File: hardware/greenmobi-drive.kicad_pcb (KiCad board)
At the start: 4 copper layers, 26 parts, among them J1 USB_C_Receptacle_USB2.0_14P, J2 Debug, J3 BAT, Q1 NMOS, SW1 RESET, SW2 BOOT, U1 STM32F405RGTx, Y1 8MHz

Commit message: Add a board edge to test CI
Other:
- board outline added: 87.1 x 77.9 mm
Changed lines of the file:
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@@
 			(psa4output no)
 			(plot_black_and_white yes)
-			(plotinvisibletext no)
 			(sketchpadsonfab no)
 			(plotpadnumbers no)
@@
 		(layer "Dwgs.User")
 	)
+	(gr_rect
+		(start 100.9 42.3)
+		(end 188 120.2)
+		(stroke
+			(width 0.05)
+			(type default)
+		)
+		(fill no)
+		(layer "Edge.Cuts")
+	)
 	(via

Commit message: half bridges
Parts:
- added C2: 2.2u, Capacitor_SMD:C_0402_1005Metric, F.Cu at (139.7, 54.8)
- added C29: 100n, Capacitor_SMD:C_1206_3216Metric, F.Cu at (123.7, 65.4)
- added C3: 2.2u, Capacitor_SMD:C_0402_1005Metric, F.Cu at (148.3, 54.8)
- added C33: 1u, Capacitor_SMD:C_0402_1005Metric, F.Cu at (133.6, 58.1)
- added C34: 4.7u, Capacitor_SMD:C_0805_2012Metric, F.Cu at (118.6, 58.6)
- added C35: 4.7u, Capacitor_SMD:C_0805_2012Metric, F.Cu at (118.6, 61.7)
- added C36: 1u, Capacitor_SMD:C_0402_1005Metric, F.Cu at (133.6, 60.1)
- added C37: 4.7u, Capacitor_SMD:C_0805_2012Metric, F.Cu at (118.6, 64.7)
- added D1: YELLOW, LED_SMD:LED_0805_2012Metric, F.Cu at (139.1, 76.7)
- added D2: RED, LED_SMD:LED_0805_2012Metric, F.Cu at (139.1, 79.8)
- added D3: GREEN, LED_SMD:LED_0805_2012Metric, F.Cu at (139.1, 82.8)
- added D4: SS34, Diode_SMD:D_SMA, F.Cu at (143.7, 96.7)
- added D5: SS34, Diode_SMD:D_SMA, F.Cu at (240.1, 85.1)
- added D6: SS34, Diode_SMD:D_SMA, F.Cu at (210.6, 85.1)
- added J2: GND, MountingHole:MountingHole_5.3mm_M5_DIN965_Pad, F.Cu at (127.2, 73.5)
- added J5: CAN, Connector_JST:JST_GH_SM04B-GHS-TB_1x04-1MP_P1.25mm_Horizontal, F.Cu at (144.1, 48.2)
- added J7: Phase_OUT, MountingHole:MountingHole_5.3mm_M5_DIN965_Pad, F.Cu at (136.4, 109.0)
- added J8: Phase_OUT, MountingHole:MountingHole_5.3mm_M5_DIN965_Pad, F.Cu at (241.4, 77.5)
- added J9: Phase_OUT, MountingHole:MountingHole_5.3mm_M5_DIN965_Pad, F.Cu at (211.9, 77.5)
- added L2: L, Inductor_SMD:L_KOHERelec_MDA7030, F.Cu at (131.0, 52.9)
- added Q10: AGM015N10LL, Package_TO_SOT_SMD:Infineon_PG-HSOF-8-1_ThermalVias, F.Cu at (228.6, 93.0)
- added Q11: AGM015N10LL, Package_TO_SOT_SMD:Infineon_PG-HSOF-8-1_ThermalVias, F.Cu at (228.6, 104.6)
- added Q12: AGM015N10LL, Package_TO_SOT_SMD:Infineon_PG-HSOF-8-1_ThermalVias, F.Cu at (228.6, 116.3)
- added Q13: AGM015N10LL, Package_TO_SOT_SMD:Infineon_PG-HSOF-8-1_ThermalVias, F.Cu at (199.1, 57.9)
- added Q14: AGM015N10LL, Package_TO_SOT_SMD:Infineon_PG-HSOF-8-1_ThermalVias, F.Cu at (199.1, 69.6)
- added Q15: AGM015N10LL, Package_TO_SOT_SMD:Infineon_PG-HSOF-8-1_ThermalVias, F.Cu at (199.1, 81.3)
- added Q16: AGM015N10LL, Package_TO_SOT_SMD:Infineon_PG-HSOF-8-1_ThermalVias, F.Cu at (199.1, 93.0)
- added Q17: AGM015N10LL, Package_TO_SOT_SMD:Infineon_PG-HSOF-8-1_ThermalVias, F.Cu at (199.1, 104.6)
- added Q18: AGM015N10LL, Package_TO_SOT_SMD:Infineon_PG-HSOF-8-1_ThermalVias, F.Cu at (199.1, 116.3)
- added Q2: AGM015N10LL, Package_TO_SOT_SMD:Infineon_PG-HSOF-8-1_ThermalVias, F.Cu at (158.2, 111.1)
- added Q3: AGM015N10LL, Package_TO_SOT_SMD:Infineon_PG-HSOF-8-1_ThermalVias, F.Cu at (168.9, 97.2)
- added Q4: AGM015N10LL, Package_TO_SOT_SMD:Infineon_PG-HSOF-8-1_ThermalVias, F.Cu at (168.9, 111.1)
- added Q5: AGM015N10LL, Package_TO_SOT_SMD:Infineon_PG-HSOF-8-1_ThermalVias, F.Cu at (179.7, 97.2)
- added Q6: AGM015N10LL, Package_TO_SOT_SMD:Infineon_PG-HSOF-8-1_ThermalVias, F.Cu at (179.7, 111.1)
- added Q7: AGM015N10LL, Package_TO_SOT_SMD:Infineon_PG-HSOF-8-1_ThermalVias, F.Cu at (228.6, 57.9)
- added Q8: AGM015N10LL, Package_TO_SOT_SMD:Infineon_PG-HSOF-8-1_ThermalVias, F.Cu at (228.6, 69.6)
- added Q9: AGM015N10LL, Package_TO_SOT_SMD:Infineon_PG-HSOF-8-1_ThermalVias, F.Cu at (228.6, 81.3)
- added R20: 56k, Resistor_SMD:R_0402_1005Metric, F.Cu at (160.0, 79.5)
- added R23: 5.1k, Resistor_SMD:R_0402_1005Metric, F.Cu at (160.0, 81.4)
- added R24: 0.2m, Resistor_SMD:R_4020_10251Metric, F.Cu at (147.1, 108.9)
- added R25: 5.1k, Resistor_SMD:R_0402_1005Metric, F.Cu at (160.0, 83.4)
- added R29: 56k, Resistor_SMD:R_0402_1005Metric, F.Cu at (237.4, 88.4)
- added R3: 56k, Resistor_SMD:R_0402_1005Metric, F.Cu at (142.7, 76.2)
- added R32: 5.1k, Resistor_SMD:R_0402_1005Metric, F.Cu at (237.4, 90.4)
- added R33: 0.2m, Resistor_SMD:R_4020_10251Metric, F.Cu at (242.3, 68.7)
- added R34: 5.1k, Resistor_SMD:R_0402_1005Metric, F.Cu at (237.4, 92.4)
- added R38: 56k, Resistor_SMD:R_0402_1005Metric, F.Cu at (207.9, 88.4)
- added R41: 5.1k, Resistor_SMD:R_0402_1005Metric, F.Cu at (207.9, 90.4)
- added R42: 0.2m, Resistor_SMD:R_4020_10251Metric, F.Cu at (212.8, 68.7)
- added R43: 5.1k, Resistor_SMD:R_0402_1005Metric, F.Cu at (207.9, 92.4)
- added R44: 82.5k, Resistor_SMD:R_0402_1005Metric, F.Cu at (130.7, 58.1)
- added R45: R, Resistor_SMD:R_0402_1005Metric, F.Cu at (130.7, 60.1)
- added R46: R, Resistor_SMD:R_0402_1005Metric, F.Cu at (130.7, 62.1)
- added R47: R, Resistor_SMD:R_0402_1005Metric, F.Cu at (130.7, 64.1)
- added U1: TJA1051T-3, Package_SO:SOIC-8_3.9x4.9mm_P1.27mm, F.Cu at (144.0, 54.8)
- added U10: AMS1117-3.3, Package_TO_SOT_SMD:SOT-223-3_TabPin2, F.Cu at (121.3, 53.0)
- added U3: IRS21867S, Package_SO:SOIC-8_3.9x4.9mm_P1.27mm, F.Cu at (154.3, 81.8)
- added U4: INA240A2D, Package_SO:SOIC-8_3.9x4.9mm_P1.27mm, F.Cu at (213.4, 102.7)
- added U5: IRS21867S, Package_SO:SOIC-8_3.9x4.9mm_P1.27mm, F.Cu at (240.2, 55.4)
- added U6: INA240A2D, Package_SO:SOIC-8_3.9x4.9mm_P1.27mm, F.Cu at (240.2, 62.0)
- added U7: IRS21867S, Package_SO:SOIC-8_3.9x4.9mm_P1.27mm, F.Cu at (210.7, 55.4)
- added U8: INA240A2D, Package_SO:SOIC-8_3.9x4.9mm_P1.27mm, F.Cu at (210.7, 62.0)
- added U9: LM5163DDA, Package_SO:HSOP-8-1EP_3.9x4.9mm_P1.27mm_EP2.41x3.1mm_ThermalVias, F.Cu at (125.0, 60.5)
- J3: value BAT -> UBAT; footprint Connector_AMASS:AMASS_XT90PW-M_1x02_P10.90mm_Horizontal -> MountingHole:MountingHole_5.3mm_M5_DIN965_Pad
- Q1: value NMOS -> AGM015N10LL
- moved Q1 50.5 mm to (158.2, 97.2), turned to 90 degrees
- moved J3 12.4 mm to (129.3, 88.1), turned to 0 degrees
- moved R12 5.68 mm to (161.7, 66.0)
- moved C12 5.68 mm to (149.8, 56.9)
- moved C4 5.68 mm to (166.2, 72.9)
- moved C6 5.68 mm to (143.3, 61.0)
- moved C7 5.68 mm to (143.3, 66.5)
- moved C9 5.68 mm to (145.6, 68.6)
- moved R13 5.68 mm to (161.7, 60.9)
- moved SW1 5.68 mm to (165.2, 55.4)
- moved SW2 5.68 mm to (165.2, 70.4)
- moved Y1 5.68 mm to (143.3, 63.8)
- moved C10 5.68 mm to (160.5, 60.9)
- moved C13 5.68 mm to (149.8, 58.0)
- moved C14 5.68 mm to (159.4, 59.9)
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- renumbered C8 to C10, C2 to C11, C7 to C12, C3 to C13, C4 to C14, C5 to C15, C6 to C16, C10 to C4, C13 to C5, C12 to C6, C11 to C7, C9 to C8, C1 to C9, J1 to J4, J2 to J6, R4 to R12, R3 to R13, R1 to R15, R2 to R16, SW2 to SW1, SW1 to SW2, U1 to U2
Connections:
- J3 pad 1: GND -> /Regulators/BAT
- Q1 pad 1: unconnected-(Q1-D-Pad1) -> Net-(Q1-G)
- Q1 pad 2: unconnected-(Q1-G-Pad2) -> Net-(Q1-S)
- Q1 pad 3: unconnected-(Q1-S-Pad3) -> /Regulators/BAT
- U2 pad 10: unconnected-(U1-PC2-Pad10) -> /half-bridge2/Current_sense
- U2 pad 11: unconnected-(U1-PC3-Pad11) -> /mcu/Vin
- U2 pad 14: unconnected-(U1-PA0-Pad14) -> /half-bridge/Phase_V_sense
- U2 pad 15: unconnected-(U1-PA1-Pad15) -> /half-bridge1/Phase_V_sense
- U2 pad 16: unconnected-(U1-PA2-Pad16) -> /half-bridge2/Phase_V_sense
- U2 pad 17: unconnected-(U1-PA3-Pad17) -> /half-bridge/TEMP
- U2 pad 24: unconnected-(U1-PC4-Pad24) -> /mcu/TEMP_MOTOR
- U2 pad 26: unconnected-(U1-PB0-Pad26) -> /half-bridge1/TEMP
- U2 pad 27: unconnected-(U1-PB1-Pad27) -> /half-bridge2/TEMP
- U2 pad 34: unconnected-(U1-PB13-Pad34) -> /half-bridge/LOW
- U2 pad 35: unconnected-(U1-PB14-Pad35) -> /half-bridge1/LOW
- U2 pad 36: unconnected-(U1-PB15-Pad36) -> /half-bridge2/LOW
- U2 pad 37: unconnected-(U1-PC6-Pad37) -> /mcu/HALL1
- U2 pad 38: unconnected-(U1-PC7-Pad38) -> /mcu/HALL2
- U2 pad 39: unconnected-(U1-PC8-Pad39) -> /mcu/HALL3
- U2 pad 41: unconnected-(U1-PA8-Pad41) -> /half-bridge/HIGH
- U2 pad 42: unconnected-(U1-PA9-Pad42) -> /half-bridge1/HIGH
- U2 pad 43: unconnected-(U1-PA10-Pad43) -> /half-bridge2/HIGH
- U2 pad 57: unconnected-(U1-PB5-Pad57) -> /mcu/LED_GREEN
- U2 pad 59: unconnected-(U1-PB7-Pad59) -> /mcu/LED_RED
- U2 pad 61: unconnected-(U1-PB8-Pad61) -> /mcu/CAN_RX
- U2 pad 62: unconnected-(U1-PB9-Pad62) -> /mcu/CAN_TX
- U2 pad 8: unconnected-(U1-PC0-Pad8) -> /half-bridge/Current_sense
- U2 pad 9: unconnected-(U1-PC1-Pad9) -> /half-bridge1/Current_sense
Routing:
- net /mcu/CAN_RX: track 0.00 -> 13.7 mm
- net /mcu/CAN_TX: track 0.00 -> 7.40 mm
- net /CAN_P: track 0.00 -> 7.09 mm
- net /CAN_N: track 0.00 -> 7.06 mm
- net +5V: track 0.00 -> 2.64 mm, vias 0 -> 1
- net +3.3V: track 18.9 -> 21.3 mm
- net GND: track 0.00 -> 1.66 mm, vias 31 -> 33

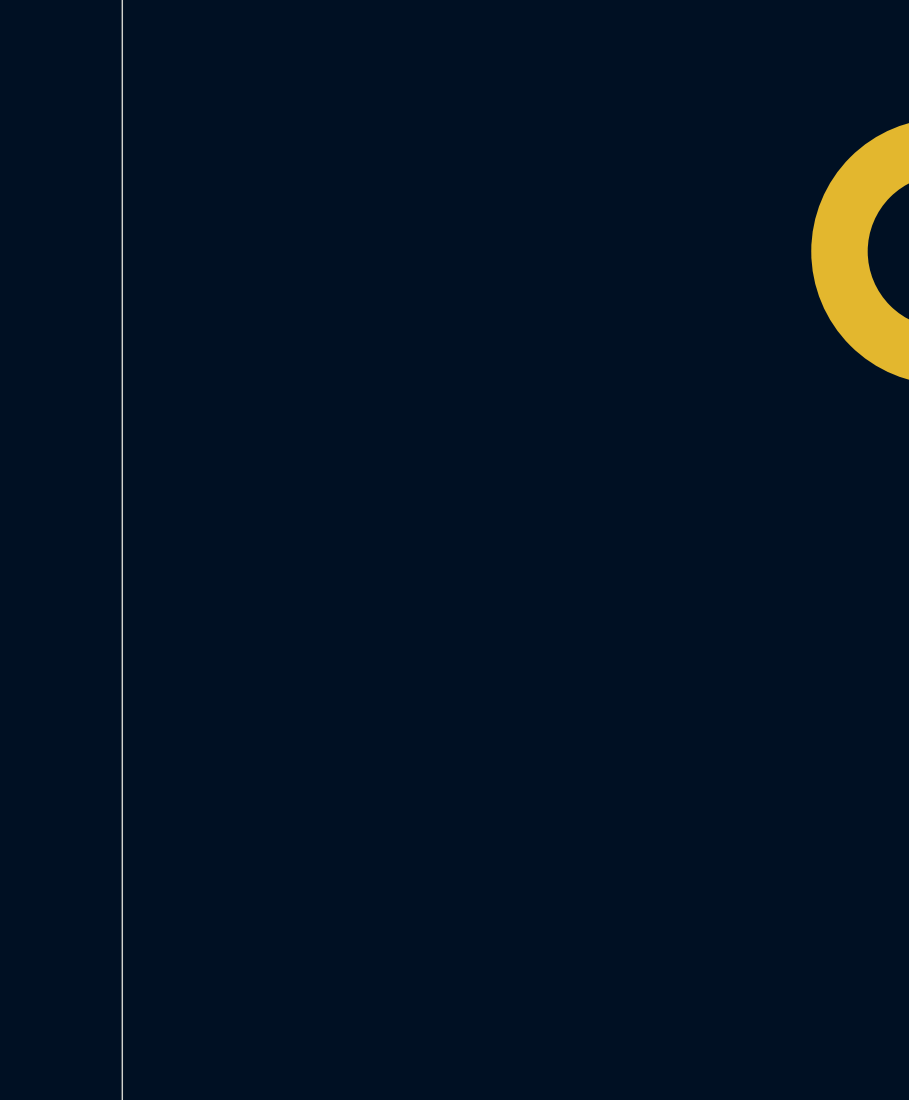
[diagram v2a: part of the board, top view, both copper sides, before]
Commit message: phase capacitors
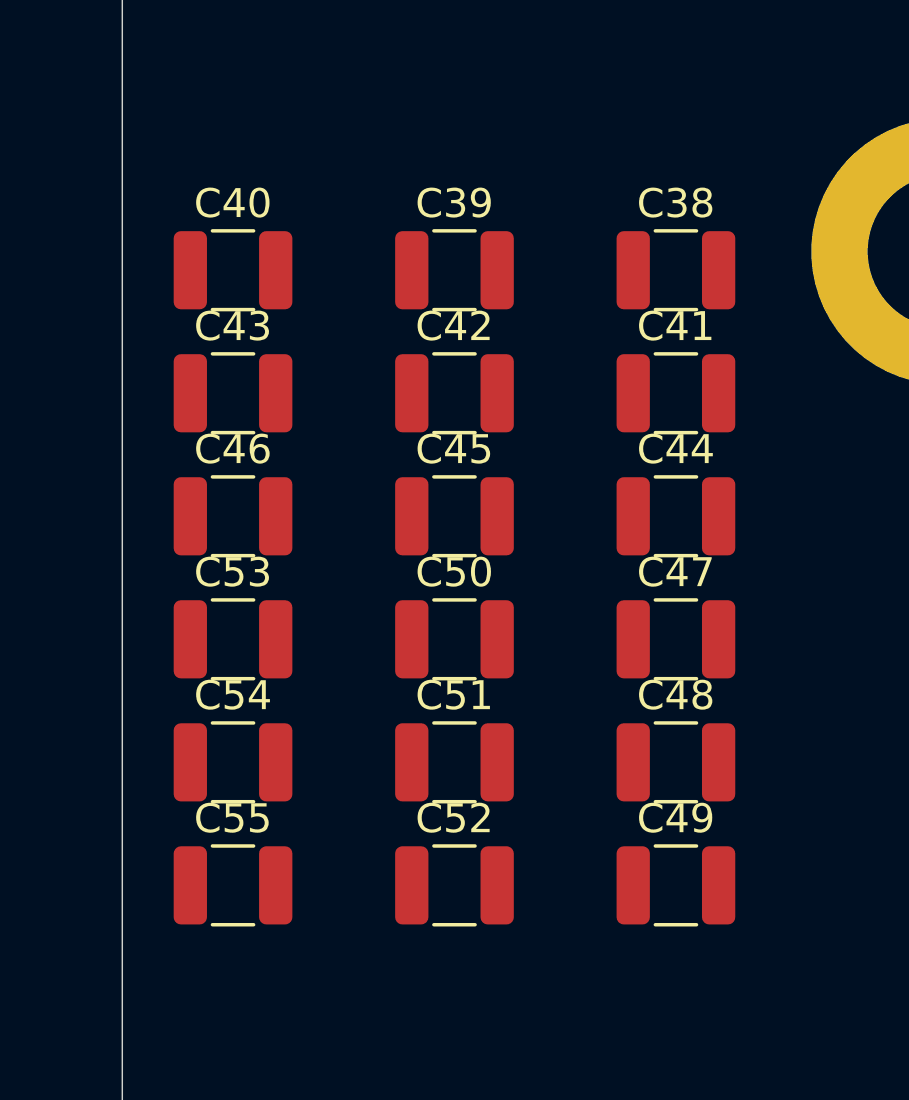
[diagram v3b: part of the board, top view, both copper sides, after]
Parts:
- added C38: 4.7u, Capacitor_SMD:C_1210_3225Metric, F.Cu at (120.0, 88.8)
- added C39: 4.7u, Capacitor_SMD:C_1210_3225Metric, F.Cu at (112.4, 88.8)
- added C40: 4.7u, Capacitor_SMD:C_1210_3225Metric, F.Cu at (104.7, 88.8)
- added C41: 4.7u, Capacitor_SMD:C_1210_3225Metric, F.Cu at (120.0, 93.0)
- added C42: 4.7u, Capacitor_SMD:C_1210_3225Metric, F.Cu at (112.4, 93.0)
- added C43: 4.7u, Capacitor_SMD:C_1210_3225Metric, F.Cu at (104.7, 93.0)
- added C44: 4.7u, Capacitor_SMD:C_1210_3225Metric, F.Cu at (120.0, 97.2)
- added C45: 4.7u, Capacitor_SMD:C_1210_3225Metric, F.Cu at (112.4, 97.2)
- added C46: 4.7u, Capacitor_SMD:C_1210_3225Metric, F.Cu at (104.7, 97.2)
- added C47: 4.7u, Capacitor_SMD:C_1210_3225Metric, F.Cu at (120.0, 101.5)
- added C48: 4.7u, Capacitor_SMD:C_1210_3225Metric, F.Cu at (120.0, 105.8)
- added C49: 4.7u, Capacitor_SMD:C_1210_3225Metric, F.Cu at (120.0, 110.0)
- added C50: 4.7u, Capacitor_SMD:C_1210_3225Metric, F.Cu at (112.4, 101.5)
- added C51: 4.7u, Capacitor_SMD:C_1210_3225Metric, F.Cu at (112.4, 105.8)
- added C52: 4.7u, Capacitor_SMD:C_1210_3225Metric, F.Cu at (112.4, 110.0)
- added C53: 4.7u, Capacitor_SMD:C_1210_3225Metric, F.Cu at (104.7, 101.5)
- added C54: 4.7u, Capacitor_SMD:C_1210_3225Metric, F.Cu at (104.7, 105.8)
- added C55: 4.7u, Capacitor_SMD:C_1210_3225Metric, F.Cu at (104.7, 110.0)

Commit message: Placement study
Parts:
- removed C38, C39, C40, C41, C42, C43, C47, C48, C50, C51, C53, C54: 4.7u, Capacitor_SMD:C_1210_3225Metric
- removed Q1, Q10, Q13, Q14, Q15, Q16, Q2, Q3, Q4, Q7, Q8, Q9: AGM015N10LL, Package_TO_SOT_SMD:Infineon_PG-HSOF-8-1_ThermalVias
- added C18: 1u, Capacitor_SMD:C_1206_3216Metric, F.Cu at (221.5, 114.2)
- added C19: 1u, Capacitor_SMD:C_0805_2012Metric, F.Cu at (220.9, 117.3)
- added C20: 100n, Capacitor_SMD:C_0402_1005Metric, F.Cu at (157.2, 150.7)
- added C22: 1u, Capacitor_SMD:C_1206_3216Metric, F.Cu at (125.9, 143.1)
- added C23: 1u, Capacitor_SMD:C_0805_2012Metric, F.Cu at (116.1, 143.9)
- added C24: 100n, Capacitor_SMD:C_0402_1005Metric, F.Cu at (132.4, 177.2)
- added C26: 1u, Capacitor_SMD:C_1206_3216Metric, F.Cu at (210.6, 114.2)
- added C27: 1u, Capacitor_SMD:C_0805_2012Metric, F.Cu at (210.0, 117.3)
- added C28: 100n, Capacitor_SMD:C_0402_1005Metric, F.Cu at (152.3, 150.7)
- added J1: Sensors, Connector_JST:JST_GH_SM06B-GHS-TB_1x06-1MP_P1.25mm_Horizontal, F.Cu at (184.8, 77.3)
- added R18: 2.2k, Resistor_SMD:R_0402_1005Metric, F.Cu at (225.7, 113.5)
- added R19: 1, Resistor_SMD:R_0805_2012Metric, F.Cu at (225.3, 117.3)
- added R21: 1, Resistor_SMD:R_0805_2012Metric, F.Cu at (149.8, 163.4)
- added R22: 1, Resistor_SMD:R_0805_2012Metric, F.Cu at (149.8, 166.4)
- added R27: 2.2k, Resistor_SMD:R_0402_1005Metric, F.Cu at (127.5, 178.3)
- added R28: 1, Resistor_SMD:R_0805_2012Metric, F.Cu at (114.1, 144.0)
- added R30: 1, Resistor_SMD:R_0805_2012Metric, F.Cu at (115.3, 141.1)
- added R31: 1, Resistor_SMD:R_0805_2012Metric, F.Cu at (115.3, 139.2)
- added R36: 2.2k, Resistor_SMD:R_0402_1005Metric, F.Cu at (214.9, 113.5)
- added R37: 1, Resistor_SMD:R_0805_2012Metric, F.Cu at (214.4, 117.3)
- added R39: 1, Resistor_SMD:R_0805_2012Metric, F.Cu at (149.8, 155.6)
- added R40: 1, Resistor_SMD:R_0805_2012Metric, F.Cu at (149.8, 158.5)
- D4, D5, D6: value SS34 -> PMEG2010EH; footprint Diode_SMD:D_SMA -> Diode_SMD:D_SOD-123F
- moved U6 160.1 mm to (132.5, 180.4)
- moved R33 150.9 mm to (129.0, 168.3)
- moved D6 149.3 mm to (81.5, 160.2)
- moved U5 148.1 mm to (120.9, 143.1), turned to 180 degrees
- moved R29 141.4 mm to (127.5, 177.3), turned to 180 degrees
- moved R34 136.5 mm to (130.5, 177.2), turned to 180 degrees
- moved J8 136.2 mm to (139.9, 168.3), turned to 180 degrees
- moved R32 134.8 mm to (134.3, 177.2)
- moved D5 125.9 mm to (128.3, 143.1), turned to -90 degrees
- moved Q12 124.8 mm to (116.1, 170.4)
- moved Q11 123.1 mm to (117.7, 158.1), turned to 90 degrees
- moved D4 94.3 mm to (79.4, 165.6), turned to 180 degrees
- moved C49 72.5 mm to (191.2, 96.2), turned to -90 degrees
- moved C44 67.8 mm to (187.8, 96.2), turned to -90 degrees
- moved C45 65.4 mm to (107.3, 162.5), turned to -90 degrees
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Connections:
- net /half-bridge/Phase_V_sense renamed /half-bridge/Phase_V
- net /half-bridge/TEMP renamed /mcu/T1
- net /half-bridge1/Phase_V_sense renamed /half-bridge1/Phase_V
- net /half-bridge1/TEMP renamed /mcu/T2
- net /half-bridge2/Phase_V_sense renamed /half-bridge2/Phase_V
- net /half-bridge2/TEMP renamed /mcu/T3
- Q11 pad 2: Net-(Q10-D) -> /half-bridge1/Center
- Q12 pad 3: Net-(Q10-D) -> /half-bridge1/Center
- Q17 pad 2: Net-(Q13-S) -> /half-bridge2/Center
- Q18 pad 3: Net-(Q13-S) -> /half-bridge2/Center
- Q5 pad 2: Net-(Q1-S) -> /half-bridge/Center
- Q6 pad 3: Net-(Q1-S) -> /half-bridge/Center
- R20 pad 2: Net-(Q1-S) -> /half-bridge/Center
- R23 pad 2: Net-(Q1-S) -> Net-(J7-Pin_1)
- R24 pad 1: Net-(J7-Pin_1) -> /half-bridge/Center
- R24 pad 2: Net-(Q1-S) -> Net-(J7-Pin_1)
- R25 pad 2: Net-(J7-Pin_1) -> /half-bridge/Center
- R29 pad 2: Net-(Q10-D) -> /half-bridge1/Center
- R32 pad 2: Net-(Q10-D) -> Net-(J8-Pin_1)
- R33 pad 1: Net-(J8-Pin_1) -> /half-bridge1/Center
- R33 pad 2: Net-(Q10-D) -> Net-(J8-Pin_1)
- R34 pad 2: Net-(J8-Pin_1) -> /half-bridge1/Center
- R38 pad 2: Net-(Q13-S) -> /half-bridge2/Center
- R41 pad 2: Net-(Q13-S) -> Net-(J9-Pin_1)
- R42 pad 1: Net-(J9-Pin_1) -> /half-bridge2/Center
- R42 pad 2: Net-(Q13-S) -> Net-(J9-Pin_1)
- R43 pad 2: Net-(J9-Pin_1) -> /half-bridge2/Center
- U3 pad 5: Net-(U3-LO) -> /half-bridge/LS
- U3 pad 7: Net-(U3-HO) -> /half-bridge/HS
- U5 pad 5: Net-(U5-LO) -> /half-bridge1/LS
- U5 pad 7: Net-(U5-HO) -> /half-bridge1/HS
- U7 pad 5: Net-(U7-LO) -> /half-bridge2/LS
- U7 pad 7: Net-(U7-HO) -> /half-bridge2/HS
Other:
- board size 87.1 x 77.9 mm -> 52.9 x 67.9 mm

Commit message: Power Layout
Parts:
- R24, R33, R42: footprint Resistor_SMD:R_4020_10251Metric -> greenmobi:R_3920
- moved D4 179.5 mm to (225.8, 61.7), turned to -90 degrees
- moved D6 162.5 mm to (224.9, 83.7), turned to -90 degrees
- moved R27 134.1 mm to (210.1, 72.6), turned to -90 degrees
- moved R29 131.8 mm to (210.0, 74.6), turned to -90 degrees
- moved U6 130.7 mm to (205.1, 71.7), turned to 180 degrees
- moved R34 126.2 mm to (205.6, 75.7), turned to 0 degrees
- moved R22 125.5 mm to (212.8, 57.8), turned to 180 degrees
- moved C24 124.0 mm to (203.8, 75.7), turned to 180 degrees
- moved R32 121.9 mm to (201.9, 75.7), turned to 180 degrees
- moved R21 121.4 mm to (212.8, 59.7), turned to 180 degrees
- moved C22 120.1 mm to (223.5, 73.2)
- moved R30 120.1 mm to (212.9, 71.2)
- moved U5 120.1 mm to (218.5, 73.2)
- moved C23 120.1 mm to (213.7, 74.0)
- moved D5 120.1 mm to (225.9, 73.2)
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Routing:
- net /mcu/RESET: track 17.7 -> 0.00 mm, vias 2 -> 0
- net +3.3V: track 21.3 -> 6.49 mm, vias 8 -> 1
- net /mcu/CAN_RX: track 13.7 -> 0.00 mm
- net /mcu/SWIO: track 9.38 -> 0.00 mm
- net /USB_DN: track 7.46 -> 0.00 mm
- net /mcu/CAN_TX: track 7.40 -> 0.00 mm
- net /USB_DP: track 7.38 -> 0.00 mm
- net Net-(U2-PH0): track 7.23 -> 0.00 mm
- net /mcu/TDI: track 6.40 -> 0.00 mm, vias 2 -> 0
- net /mcu/SWO: track 5.86 -> 0.00 mm
- net Net-(U2-PH1): track 5.34 -> 0.00 mm
- net /mcu/SWCLK: track 5.21 -> 0.00 mm
- net /mcu/VDDA: track 4.48 -> 0.00 mm
- net Net-(J4-CC1): track 2.54 -> 0.00 mm
- net Net-(U2-VCAP_2): track 2.03 -> 0.00 mm
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- added copper zone on F.Cu, net /Regulators/BAT
- added copper zone on F.Cu, net Net-(J7-Pin_1)
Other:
- board size 52.9 x 67.9 mm -> 100 x 70.6 mm

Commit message: Layout
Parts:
- removed D1: YELLOW, LED_SMD:LED_0805_2012Metric
- removed D2: RED, LED_SMD:LED_0805_2012Metric
- added C1: 100n, Capacitor_SMD:C_0402_1005Metric, F.Cu at (117.5, 72.0)
- added C17: 100n, Capacitor_SMD:C_0402_1005Metric, F.Cu at (123.5, 72.4)
- added C25: 100n, Capacitor_SMD:C_0402_1005Metric, F.Cu at (123.5, 68.5)
- added C38: 100n, Capacitor_SMD:C_0402_1005Metric, F.Cu at (123.5, 64.5)
- added D7: GREEN, LED_SMD:LED_1210_3225Metric, F.Cu at (177.8, 75.0)
- added D8: Red, LED_SMD:LED_1210_3225Metric, F.Cu at (177.9, 82.3)
- added H1: Heatsink, MountingHole:MountingHole_3.2mm_M3_Pad, F.Cu at (189.9, 142.0)
- added H2: Heatsink, MountingHole:MountingHole_3.2mm_M3_Pad, F.Cu at (98.4, 50.4)
- added H3: Heatsink, MountingHole:MountingHole_3.2mm_M3_Pad, F.Cu at (189.1, 50.6)
- added H4: Heatsink, MountingHole:MountingHole_3.2mm_M3_Pad, F.Cu at (97.7, 141.9)
- added H5: Heatsink, MountingHole:MountingHole_3.2mm_M3_Pad, F.Cu at (144.2, 92.2)
- added Q2: MMBT3904, Package_TO_SOT_SMD:SOT-23, F.Cu at (172.8, 75.0)
- added Q3: MMBT3904, Package_TO_SOT_SMD:SOT-23, F.Cu at (172.7, 82.3)
- added R1: 0, Resistor_SMD:R_0402_1005Metric, F.Cu at (114.6, 64.5)
- added R11: 68, Resistor_SMD:R_0603_1608Metric, F.Cu at (182.4, 67.4)
- added R14: 120, Resistor_SMD:R_0402_1005Metric, F.Cu at (137.9, 53.3)
- added R17: 15, Resistor_SMD:R_0603_1608Metric, F.Cu at (182.4, 75.0)
- added R35: 68, Resistor_SMD:R_0603_1608Metric, F.Cu at (182.4, 82.3)
- added R4: 0, Resistor_SMD:R_0402_1005Metric, F.Cu at (114.6, 66.5)
- added R6: 2.2k, Resistor_SMD:R_0805_2012Metric, F.Cu at (159.6, 102.8)
- added R8: 10k, Resistor_SMD:R_0402_1005Metric, F.Cu at (114.6, 68.5)
- added TH2: 10k, Resistor_SMD:R_0402_1005Metric, F.Cu at (114.6, 72.5)
- D3: value GREEN -> Yellow; footprint LED_SMD:LED_0805_2012Metric -> LED_SMD:LED_1210_3225Metric
- R24, R33, R42: footprint greenmobi:R_3920 -> Resistor_SMD:R_2512_6332Metric
- R3: footprint Resistor_SMD:R_0402_1005Metric -> Resistor_SMD:R_0805_2012Metric
- moved R36 103.4 mm to (107.4, 101.9)
- moved R41 103.4 mm to (100.5, 104.3)
- moved C26 103.4 mm to (120.8, 102.5)
- moved D6 103.4 mm to (123.2, 102.5)
- moved U7 103.4 mm to (115.8, 102.5)
- moved U8 103.4 mm to (102.4, 101.0)
- moved C27 103.4 mm to (111.0, 103.3)
- moved C28 103.4 mm to (102.4, 104.3)
- moved R37 103.4 mm to (109.0, 103.4)
- moved R38 103.4 mm to (107.3, 103.9)
- moved R39 103.4 mm to (110.2, 100.5)
- moved R40 103.4 mm to (110.2, 98.6)
- moved R43 103.4 mm to (104.2, 104.2)
- moved U4 83.9 mm to (131.4, 100.6)
- moved C20 83.9 mm to (131.4, 103.8)
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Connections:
- J1 pad MP: (no net) -> GND
- J5 pad MP: (no net) -> GND
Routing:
- net /Regulators/BAT: track 0.00 -> 13.1 mm
- net /CAN_P: track 7.09 -> 9.13 mm
- net /CAN_N: track 7.06 -> 8.39 mm
- added copper zone on F.Cu, net /half-bridge/Center
- added copper zone on F.Cu, net /half-bridge1/Center
- added copper zone on F.Cu, net /half-bridge2/Center
- added copper zone on F.Cu, net Net-(J8-Pin_1)
- removed copper zone on In1.Cu, net GND
- removed copper zone on F.Cu, net Net-(J7-Pin_1)
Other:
- board size 100 x 70.6 mm -> 100 x 100 mm
- copper layers 4 -> 2

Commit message: Added IMU
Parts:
- added C21: 2.2u, Capacitor_SMD:C_0402_1005Metric, F.Cu at (107.9, 62.2)
- added C30: 2.2n, Capacitor_SMD:C_0402_1005Metric, F.Cu at (109.0, 55.2)
- added C31: 56p, Capacitor_SMD:C_0603_1608Metric, F.Cu at (105.5, 55.5)
- added C32: 3.3n, Capacitor_SMD:C_0603_1608Metric, F.Cu at (105.5, 58.0)
- added C39: 100n, Capacitor_SMD:C_0402_1005Metric, F.Cu at (134.3, 81.1)
- added C40: 100n, Capacitor_SMD:C_0402_1005Metric, F.Cu at (134.3, 83.1)
- added R2: 2.2k, Resistor_SMD:R_0402_1005Metric, F.Cu at (105.0, 62.2)
- added R26: 5.1k, Resistor_SMD:R_0402_1005Metric, F.Cu at (105.0, 68.2)
- added R5: 2.2k, Resistor_SMD:R_0402_1005Metric, F.Cu at (105.0, 64.2)
- added R7: 2.2k, Resistor_SMD:R_0402_1005Metric, F.Cu at (105.0, 66.2)
- added U11: BMI323, Package_LGA:Bosch_LGA-14_3x2.5mm_P0.5mm, F.Cu at (130.5, 82.4)
- L2: value L -> 6.8u
- R45, R46: value R -> 453k; footprint Resistor_SMD:R_0402_1005Metric -> Resistor_SMD:R_0603_1608Metric
- R47: value R -> 49.9
- R6: footprint Resistor_SMD:R_0805_2012Metric -> Resistor_SMD:R_0402_1005Metric
